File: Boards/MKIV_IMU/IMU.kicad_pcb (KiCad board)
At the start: 2 copper layers, 17 parts, among them U2 TPS561201

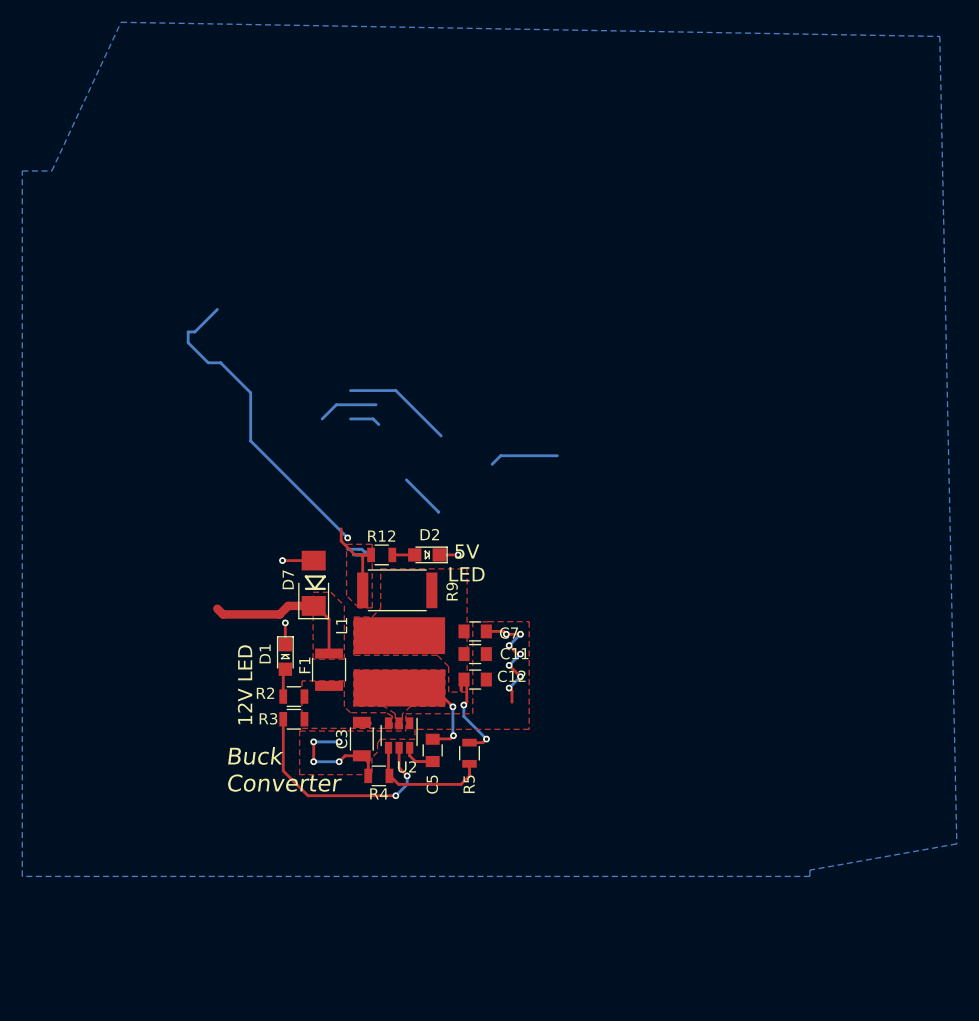
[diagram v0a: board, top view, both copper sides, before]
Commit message: Updated IMU board
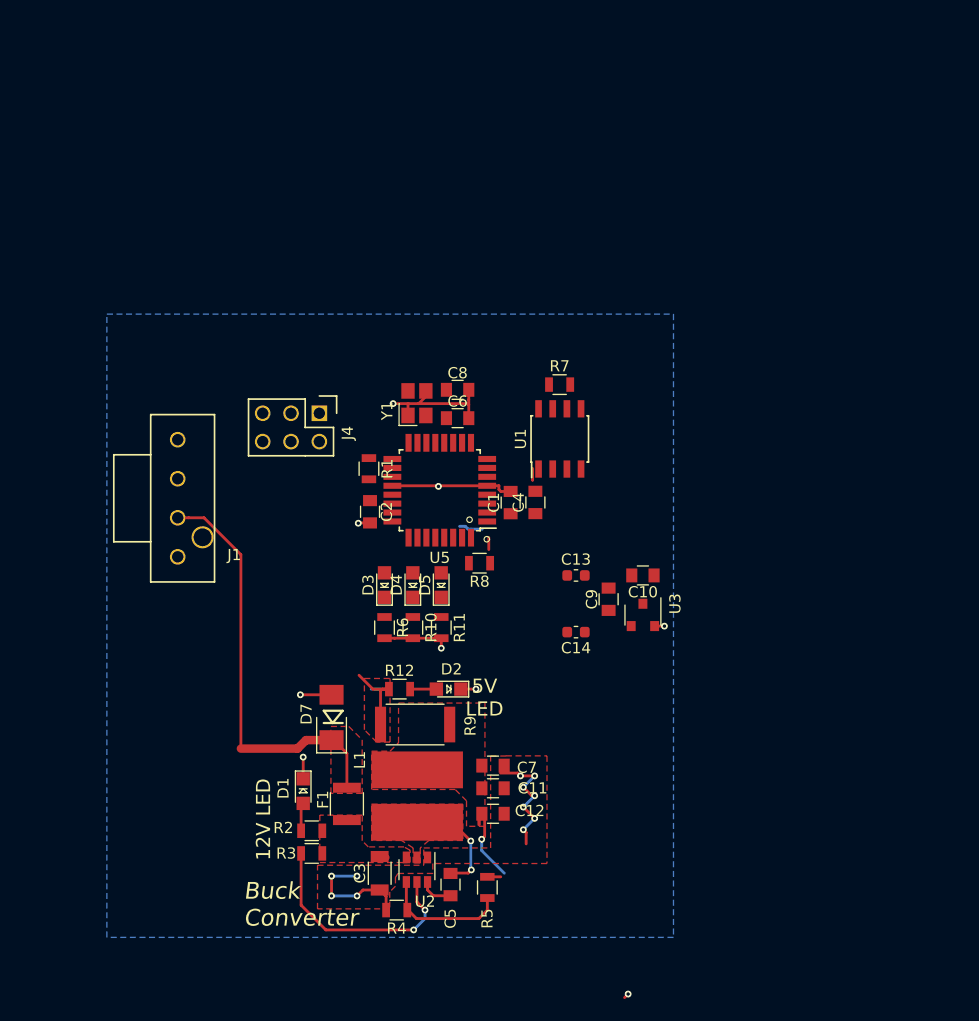
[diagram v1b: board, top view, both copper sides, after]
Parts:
- added C1: C_0.1uF, footprints:C_0805_OEM, F.Cu at (151.8, 88.0)
- added C10: C_0.1uF, footprints:C_0805_OEM, F.Cu at (163.6, 94.5)
- added C13: C_100nF, footprints:C_0603_1608Metric, F.Cu at (157.6, 94.6)
- added C14: C_100nF, footprints:C_0603_1608Metric, F.Cu at (157.6, 99.6)
- added C2: C_100pF, footprints:C_0805_OEM, F.Cu at (139.2, 88.8)
- added C4: C_0.1uF, footprints:C_0805_OEM, F.Cu at (154.0, 88.0)
- added C6: C_30pF, footprints:C_0805_OEM, F.Cu at (147.0, 80.4)
- added C8: C_30pF, footprints:C_0805_OEM, F.Cu at (147.0, 77.9)
- added C9: C_0.1uF, footprints:C_0805_OEM, F.Cu at (160.6, 96.7)
- added D3: LED_0805, footprints:LED_0805_OEM, F.Cu at (140.5, 95.4)
- added D4: LED_0805, footprints:LED_0805_OEM, F.Cu at (143.0, 95.4)
- added D5: LED_0805, footprints:LED_0805_OEM, F.Cu at (145.5, 95.4)
- added J1: UF_4_VT, footprints:Ultrafit_4, F.Cu at (121.9, 87.6)
- added J4: CONN_02X03, footprints:Pin_Header_Straight_2x03, F.Cu at (134.6, 80.0)
- added R1: R_100, footprints:R_0805_OEM, F.Cu at (139.1, 85.0)
- added R10: R_200, footprints:R_0805_OEM, F.Cu at (143.0, 99.2)
- added R11: R_200, footprints:R_0805_OEM, F.Cu at (145.6, 99.2)
- added R6: R_200, footprints:R_0805_OEM, F.Cu at (140.5, 99.2)
- added R7: R_200, footprints:R_0805_OEM, F.Cu at (156.2, 77.4)
- added R8: R_10k, footprints:R_0805_OEM, F.Cu at (149.0, 93.5)
- added U1: CAN_Transceiver, footprints:SOIC-8_3.9x4.9mm_Pitch1.27mm_OEM, F.Cu at (156.2, 82.3)
- added U3: LM3480, footprints:SOT-23-3_OEM, F.Cu at (163.6, 97.1)
- added U5: ATMEGA16M1, footprints:TQFP-32_7x7mm_Pitch0.8mm, F.Cu at (145.4, 86.9)
- added Y1: Crystal_SMD, footprints:Crystal_SMD_FA238, F.Cu at (143.4, 79.1)
- moved D2 12.2 mm to (146.2, 104.7)
- moved C11 12.1 mm to (150.2, 113.6)
- moved C12 12.1 mm to (150.2, 115.9)
- moved C3 12.1 mm to (140.0, 121.3)
- moved C7 12.1 mm to (150.2, 111.6)
- moved D1 12.1 mm to (133.2, 113.9)
- moved D7 12.1 mm to (135.7, 107.3)
- moved F1 12.1 mm to (137.1, 115.0)
- moved R12 12.1 mm to (141.8, 104.7)
- moved R2 12.1 mm to (133.9, 117.4)
- moved R3 12.1 mm to (133.9, 119.5)
- moved R5 12.1 mm to (149.7, 122.5)
- moved R9 12.1 mm to (143.2, 107.9)
- moved C5 12.1 mm to (146.4, 122.3)
- moved L1 12.1 mm to (143.4, 114.3)
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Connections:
- net +12V renamed /12V
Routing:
- net /12V: track 14.1 -> 37.8 mm
- net VCC: track 19.6 -> 8.14 mm
- net /SCK: track 9.81 -> 0.00 mm
- net /RXCAN: track 4.11 -> 0.00 mm
- net GND: track 61.2 -> 65.0 mm, vias 15 -> 20
- net /MISO: track 2.75 -> 0.00 mm
- net Net-(C11-Pad1): track 12.1 -> 11.6 mm, vias 2 -> 1
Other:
- board text added: "For Instructional Use Only."
- board text added: "SOLIDWORKS Educational Product."

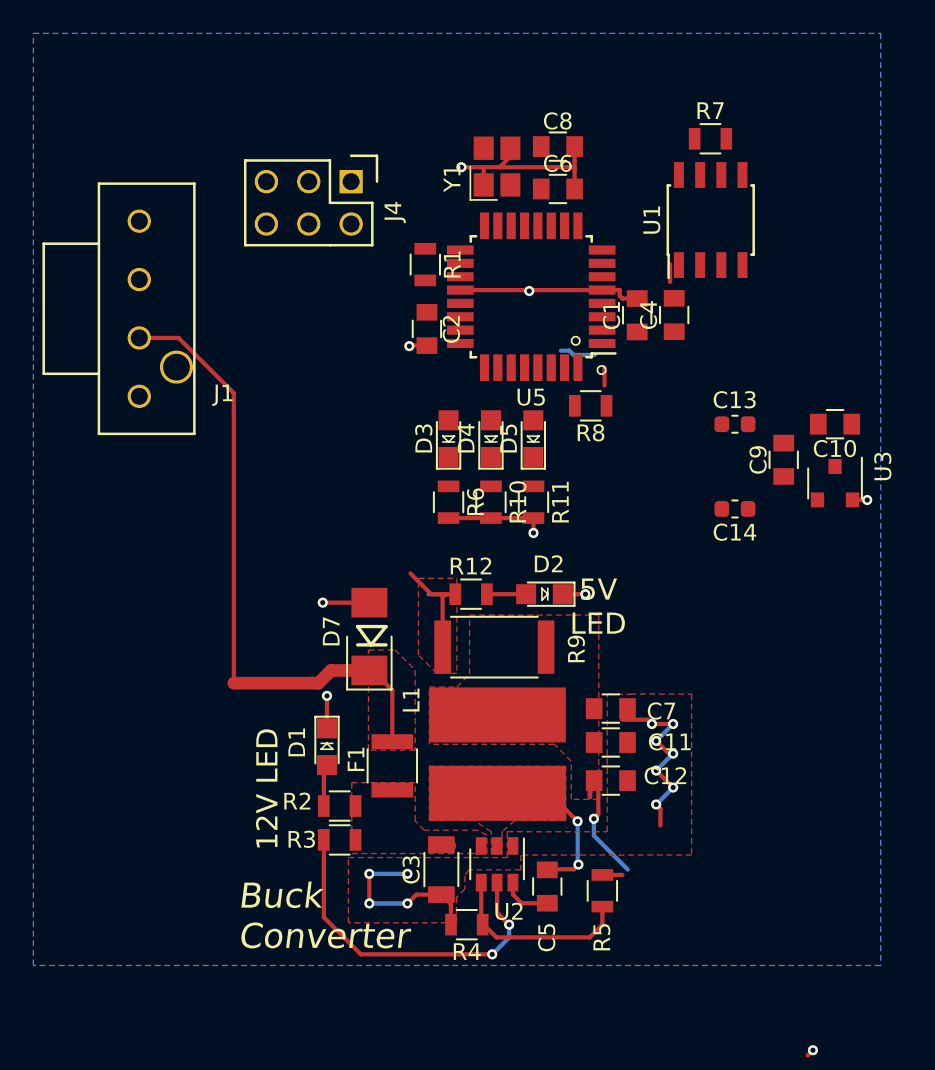
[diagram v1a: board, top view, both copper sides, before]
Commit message: Updated PCB IMU
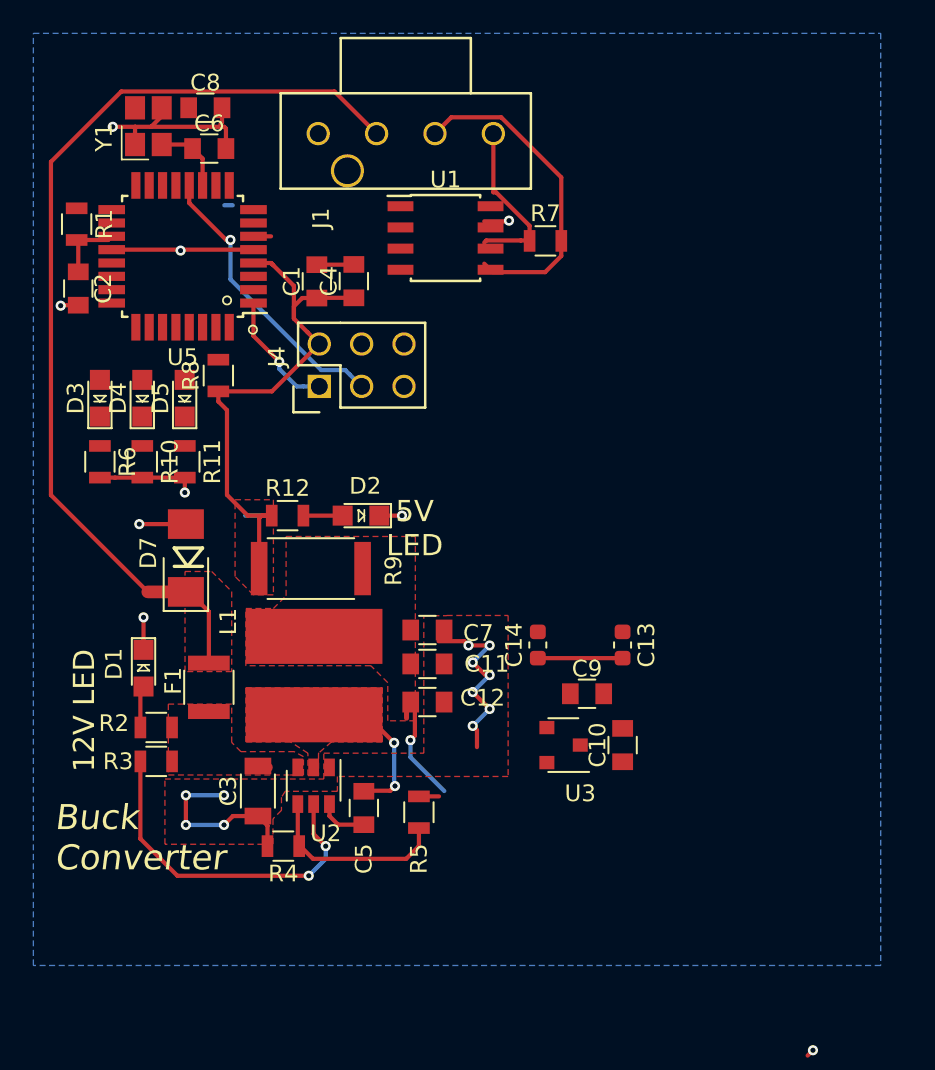
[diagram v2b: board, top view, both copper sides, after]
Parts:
- moved C10 23.1 mm to (150.9, 113.8), turned to 90 degrees
- moved U3 22.6 mm to (148.4, 113.8), turned to 180 degrees
- moved R8 22.4 mm to (126.7, 91.6), turned to 90 degrees
- moved C8 21.3 mm to (125.9, 75.6)
- moved D5 21.0 mm to (124.6, 93.0)
- moved R11 21.0 mm to (124.7, 96.8)
- moved C2 21.0 mm to (118.3, 86.4)
- moved C6 21.0 mm to (126.1, 78.0)
- moved D3 21.0 mm to (119.6, 93.0)
- moved D4 21.0 mm to (122.1, 93.0)
- moved R1 21.0 mm to (118.2, 82.6)
- moved R10 21.0 mm to (122.1, 96.8)
- moved R6 21.0 mm to (119.6, 96.8)
- moved U5 21.0 mm to (124.5, 84.5)
- moved Y1 21.0 mm to (122.5, 76.7)
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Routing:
- net VCC: track 8.14 -> 32.5 mm
- net /12V: track 37.8 -> 57.7 mm
- net /CANL: track 0.00 -> 19.4 mm
- net /SCK: track 0.00 -> 17.3 mm, vias 0 -> 1
- net /CANH: track 0.00 -> 9.97 mm
- net /MISO: track 0.00 -> 7.42 mm, vias 0 -> 1
- net /3.3V: track 0.00 -> 5.08 mm
- net Net-(C6-Pad1): track 0.00 -> 4.41 mm
- net Net-(C2-Pad1): track 0.00 -> 4.14 mm
- net GND: track 65.0 -> 62.0 mm
- net /TXCAN: track 0.00 -> 1.05 mm
- net /MOSI2: track 0.00 -> 0.51 mm

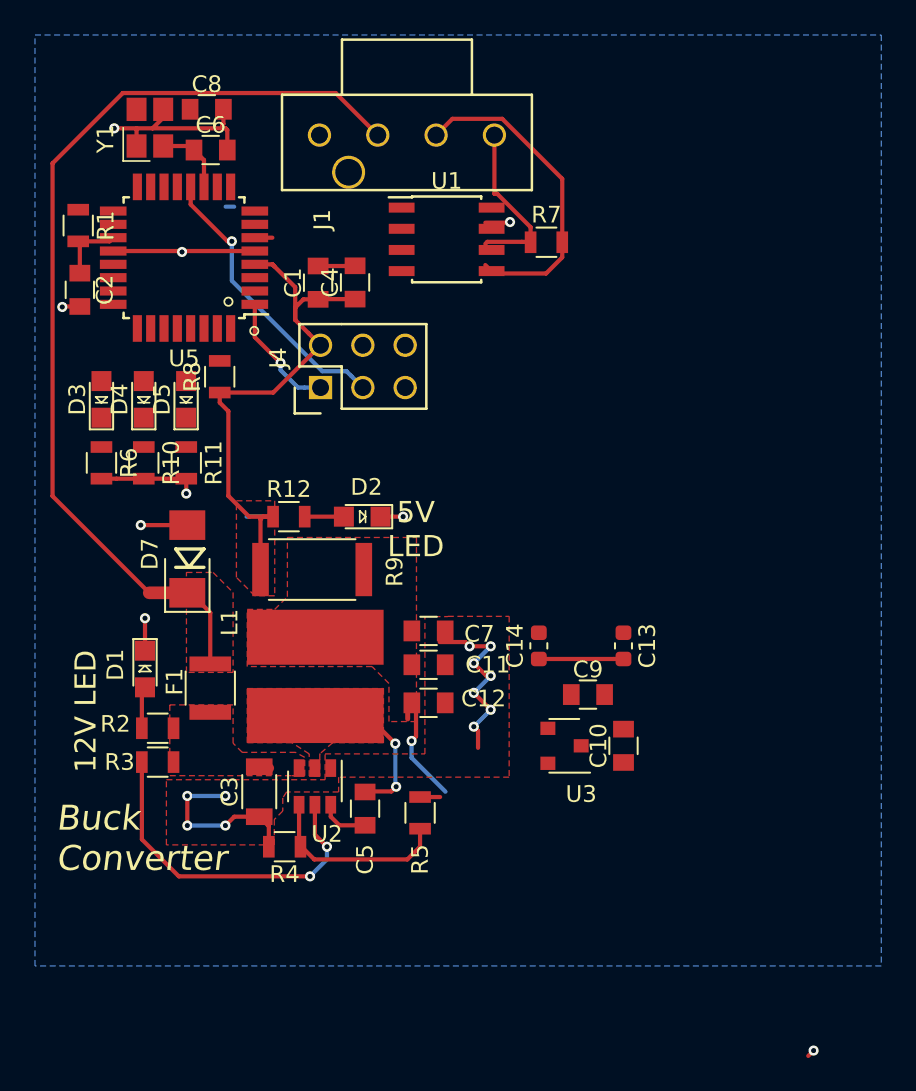
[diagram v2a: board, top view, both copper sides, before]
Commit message: Updated CAN end resistor and added BMI088 footprint and other stuff
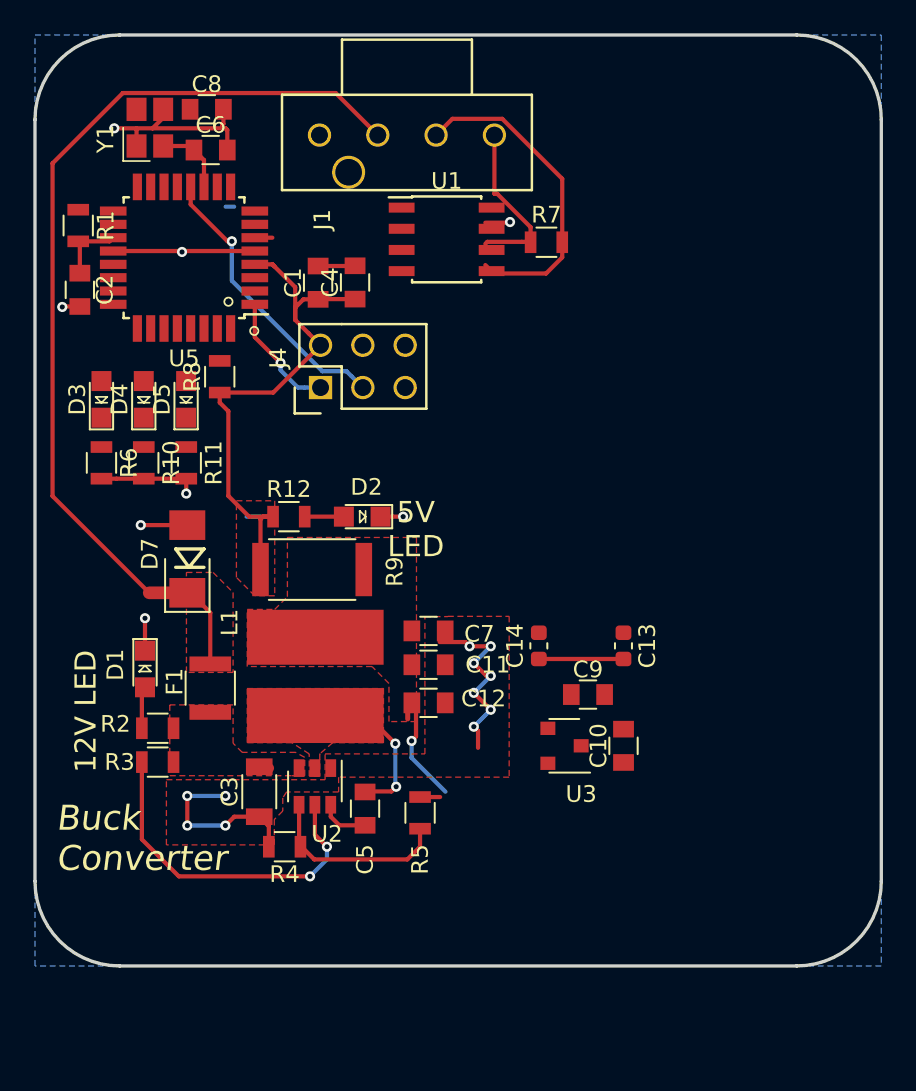
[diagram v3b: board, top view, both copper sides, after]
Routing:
- net GND: track 62.0 -> 61.5 mm, vias 20 -> 19
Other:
- board outline added: 50.8 x 55.9 mm
- board text removed: "For Instructional Use Only."
- board text removed: "SOLIDWORKS Educational Product."
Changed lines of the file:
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@@
   (general
     (thickness 1.6)
-    (drawings 13)
-    (tracks 195)
+    (drawings 11)
+    (tracks 193)
     (zones 0)
     (modules 41)
@@
   (layers
     (0 F.Cu signal)
-    (31 B.Cu signal)
+    (31 B.Cu signal hide)
     (32 B.Adhes user)
     (33 F.Adhes user)
@@
     (trace_min 0.2)
     (segment_width 0.2)
-    (edge_width 0.15)
+    (edge_width 0.2)
     (via_size 0.6096)
     (via_drill 0.3048)
@@
     )
   )
-  (gr_line (start 161.29 71.12) (end 120.65 71.12) (layer Dwgs.User) (width 0.2))
-  (gr_text "For Instructional Use Only." (at 115.57 135.269996) (layer Dwgs.User)
-    (effects (font (size 4.83362 3.866896) (thickness 0.2)) (justify left top))
-  )
-  (gr_arc (start 120.65 121.92) (end 115.57 121.92) (angle -90) (layer Dwgs.User) (width 0.2))
-  (gr_text "SOLIDWORKS Educational Product." (at 115.57 128.019566) (layer Dwgs.User)
-    (effects (font (size 4.83362 3.866896) (thickness 0.2)) (justify left top))
-  )
-  (gr_line (start 120.65 127) (end 161.29 127) (layer Dwgs.User) (width 0.2))
-  (gr_line (start 115.57 76.2) (end 115.57 121.92) (layer Dwgs.User) (width 0.2))
-  (gr_line (start 166.37 121.92) (end 166.37 76.2) (layer Dwgs.User) (width 0.2))
-  (gr_arc (start 120.65 76.2) (end 120.65 71.12) (angle -90) (layer Dwgs.User) (width 0.2))
-  (gr_arc (start 161.29 76.2) (end 166.37 76.2) (angle -90) (layer Dwgs.User) (width 0.2))
-  (gr_arc (start 161.29 121.92) (end 161.29 127) (angle -90) (layer Dwgs.User) (width 0.2))
+  (gr_line (start 161.29 71.12) (end 120.65 71.12) (layer Edge.Cuts) (width 0.2))
+  (gr_arc (start 120.65 121.92) (end 115.57 121.92) (angle -90) (layer Edge.Cuts) (width 0.2))
+  (gr_line (start 120.65 127) (end 161.29 127) (layer Edge.Cuts) (width 0.2))
+  (gr_line (start 115.57 76.2) (end 115.57 121.92) (layer Edge.Cuts) (width 0.2))
+  (gr_line (start 166.37 121.92) (end 166.37 76.2) (layer Edge.Cuts) (width 0.2))
+  (gr_arc (start 120.65 76.2) (end 120.65 71.12) (angle -90) (layer Edge.Cuts) (width 0.2))
+  (gr_arc (start 161.29 76.2) (end 166.37 76.2) (angle -90) (layer Edge.Cuts) (width 0.2))
+  (gr_arc (start 161.29 121.92) (end 161.29 127) (angle -90) (layer Edge.Cuts) (width 0.2))
   (gr_text "Buck\nConverter" (at 116.8398 119.33584) (layer F.SilkS)
     (effects (font (size 1.5 1.5) (thickness 0.2032) italic) (justify left))
@@
   (segment (start 129.5398 100.03184) (end 128.2698 100.03184) (width 0.254) (layer B.Cu) (net 1))
   (segment (start 129.7938 99.77784) (end 129.5398 100.03184) (width 0.254) (layer B.Cu) (net 1))
-  (segment (start 127.52324 81.42732) (end 127.01524 81.42732) (width 0.254) (layer B.Cu) (net 34))
   (segment (start 124.7138 116.79584) (end 126.9998 116.79584) (width 0.254) (layer B.Cu) (net 1))
   (segment (start 126.9998 118.57384) (end 124.7138 118.57384) (width 0.254) (layer B.Cu) (net 1))
@@
   (via (at 121.9198 100.53984) (size 0.6096) (drill 0.3048) (layers F.Cu B.Cu) (net 1))
   (segment (start 124.7138 100.53984) (end 121.9198 100.53984) (width 0.254) (layer F.Cu) (net 1))
-  (segment (start 161.986 132.4) (end 162.306 132.08) (width 0.254) (layer F.Cu) (net 1))
-  (via (at 162.306 132.08) (size 0.6096) (drill 0.3048) (layers F.Cu B.Cu) (net 1))
   (segment (start 120.4641 97.752771) (end 122.1001 97.752771) (width 0.254) (layer F.Cu) (net 1))
   (segment (start 119.5601 97.752771) (end 120.4641 97.752771) (width 0.254) (layer F.Cu) (net 1))
@@
   (segment (start 143.1466 80.64796) (end 143.30948 80.64796) (width 0.254) (layer F.Cu) (net 27))
   (segment (start 129.819029 83.287436) (end 128.765029 83.287436) (width 0.254) (layer F.Cu) (net 30))
+  (segment (start 127.52324 81.42732) (end 127.01524 81.42732) (width 0.254) (layer B.Cu) (net 34))
   (zone (net 7) (net_name /12V_Fused) (layer F.Cu) (hatch edge 0.508)
     (connect_pads yes (clearance 0.1524))

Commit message: Updated schematic and layout and net list
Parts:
- added U4: BMI088, footprints:bmi088, F.Cu at (152.3, 85.4)
- R7: value R_200 -> R_120
- moved U3 31.7 mm to (161.8, 85.1), turned to 90 degrees
- moved C10 29.0 mm to (158.7, 85.9), turned to 270 degrees
- moved J1 27.2 mm to (122.3, 99.4), turned to 0 degrees
- moved C9 26.9 mm to (161.6, 87.1), turned to 180 degrees
- moved C14 24.7 mm to (156.9, 85.7), turned to 270 degrees
- moved C13 22.5 mm to (155.3, 85.7), turned to 90 degrees
- moved C1 20.7 mm to (149.9, 97.3), turned to 270 degrees
- moved C5 18.4 mm to (153.8, 118.3)
- moved R12 18.4 mm to (149.2, 100.8)
- moved R5 18.4 mm to (157.1, 118.6)
- moved R8 18.4 mm to (145.1, 92.4)
- moved R9 18.4 mm to (150.6, 104.0)
- moved U5 18.4 mm to (142.9, 85.3)
- moved D7 18.4 mm to (143.1, 103.3)
- moved F1 18.4 mm to (144.5, 111.1)
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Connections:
- J1 pad 3: /CANL -> /CANH
- J1 pad 4: /CANH -> /CANL
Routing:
- net VCC: track 32.5 -> 97.6 mm, vias 0 -> 2
- net /INT4: track 0.00 -> 34.4 mm, vias 0 -> 2
- net /CS_GYRO: track 0.00 -> 32.5 mm, vias 0 -> 2
- net /12V: track 57.7 -> 27.6 mm
- net /CANH: track 9.97 -> 33.5 mm
- net /INT2: track 0.00 -> 22.9 mm, vias 0 -> 2
- net /INT1: track 0.00 -> 19.4 mm, vias 0 -> 2
- net GND: track 61.5 -> 80.3 mm, vias 19 -> 23
- net /SCK: track 17.3 -> 35.4 mm
- net /RESET: track 0.00 -> 14.9 mm, vias 0 -> 1
- net /CANL: track 19.4 -> 33.0 mm
- net /CS_ACCEL: track 0.00 -> 13.3 mm, vias 0 -> 2
- net /INT3: track 0.00 -> 12.8 mm, vias 0 -> 2
- net /RXCAN: track 0.00 -> 12.5 mm
- net /SCK2: track 0.00 -> 12.5 mm, vias 0 -> 2
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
